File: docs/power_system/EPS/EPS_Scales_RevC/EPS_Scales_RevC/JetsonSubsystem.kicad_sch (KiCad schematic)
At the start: 19 parts, among them U4 INA230

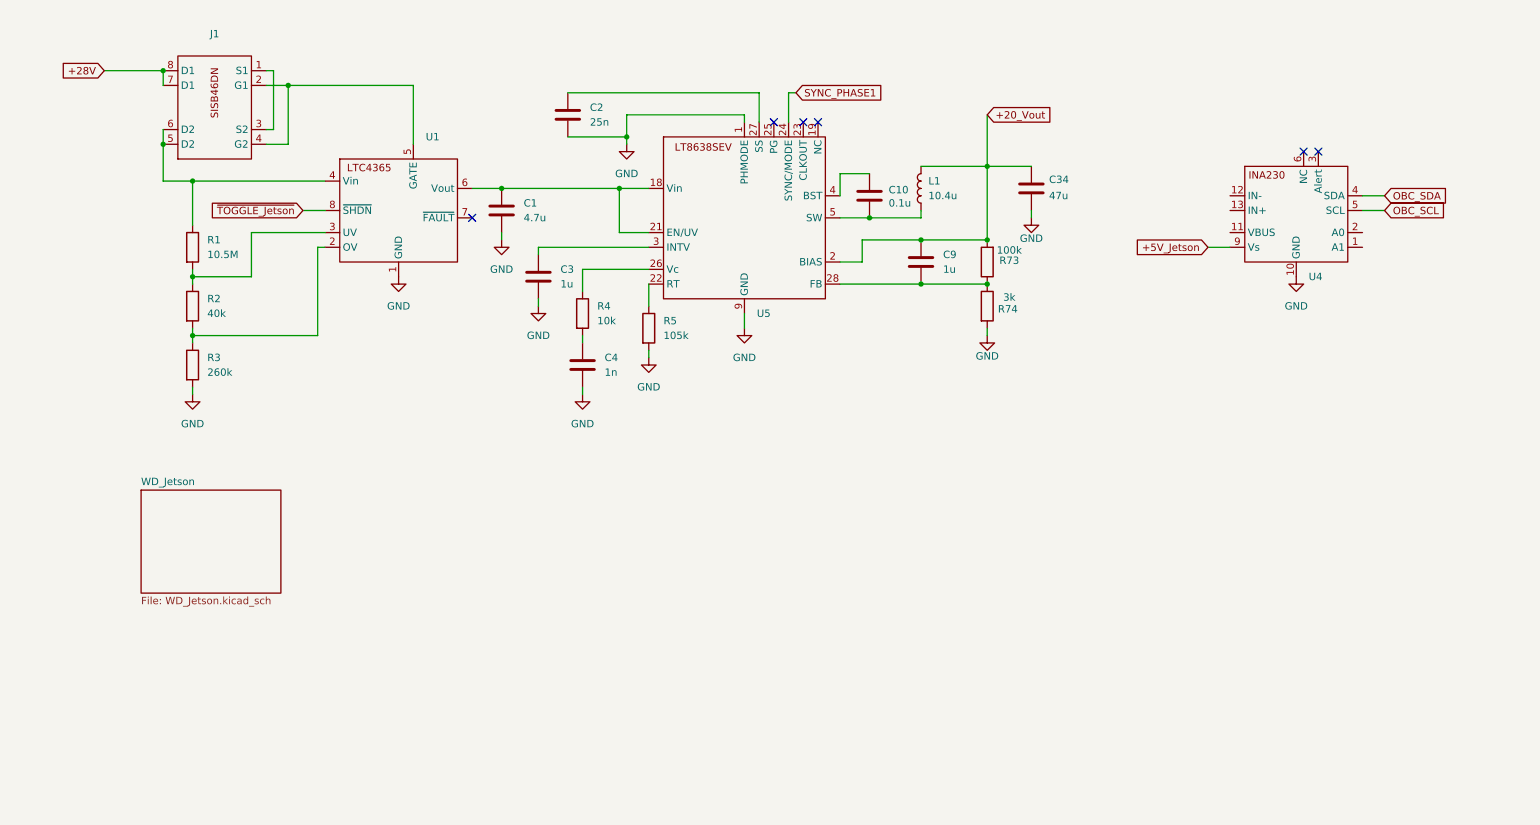
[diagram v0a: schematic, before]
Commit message: Calculations
Lots of behind the scenes stuff going on. Ran through calculations for the Load Switch, Switching Regulator and clock for the jetson using the information from each datasheet. Having to modify these parameters for each subsystem is time consuming as each one requires new calculations. Once this bit is done the schematic will be done, leading to layout. Aiming for thursday Layout.
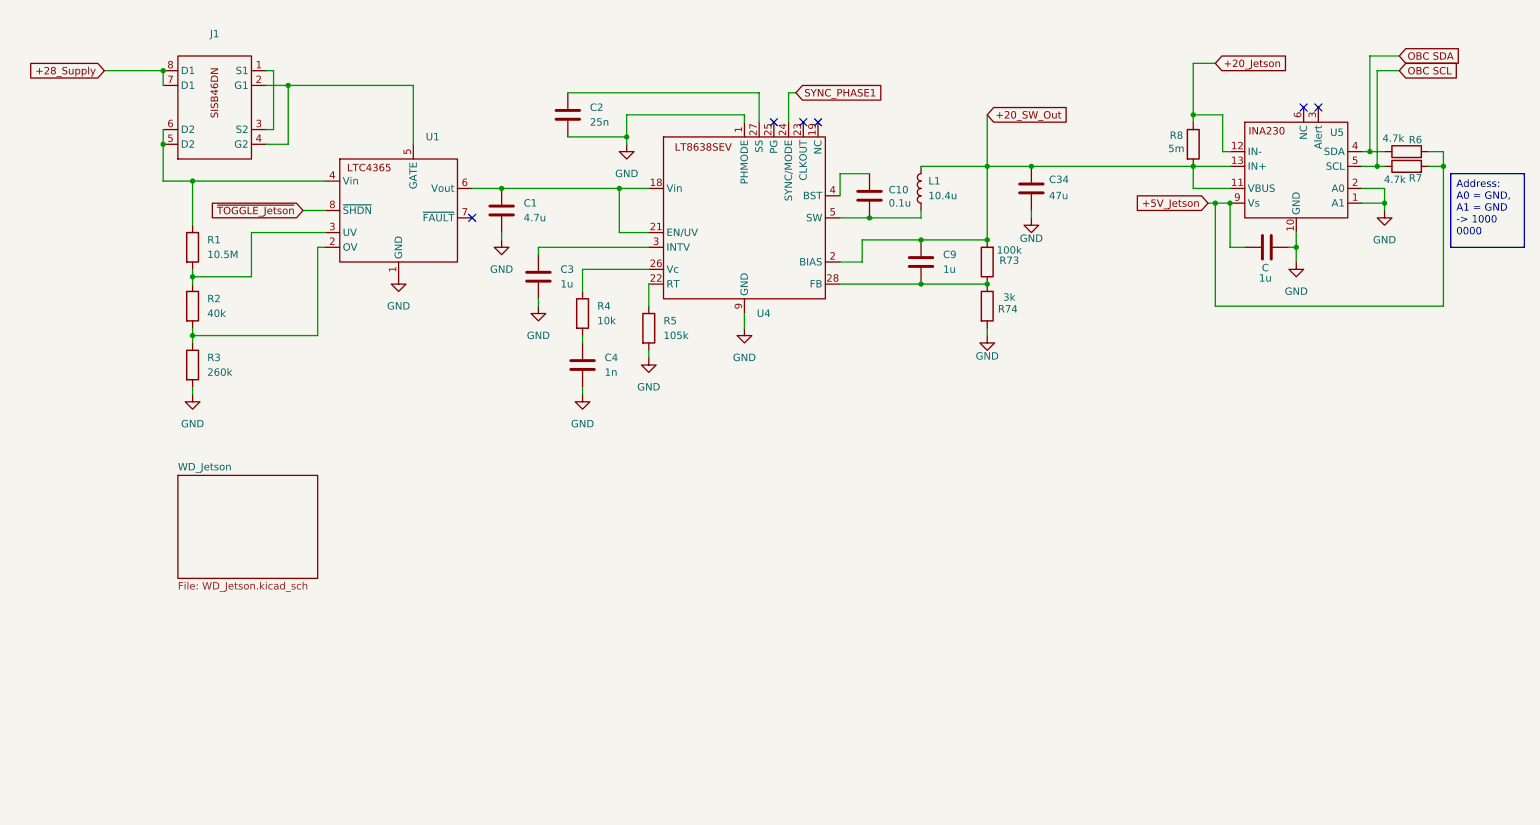
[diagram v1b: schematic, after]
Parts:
- removed U4: INA230, RevC Footprints:INA230AIRGTT, symbol INA230:INA230 [RGT PACKAGE]
- removed U5: ~, RevC Footprints:LT8638SEVPBF, symbol LT8638SEV#PBF:LT863SEV#PBF
- added 1u: C, symbol Device:C
- added R6, R7: 4.7k, symbol Device:R
- added R8: 5m, symbol Device:R
- added U4: ~, RevC Footprints:LT8638SEVPBF, symbol LT8638SEV#PBF:LT863SEV#PBF
- added U5: INA230, RevC Footprints:INA230AIRGTT, symbol INA230:INA230 [RGT PACKAGE]
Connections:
- net +5V_Jetson: now also 1u.2, R6.2, R7.2, U5.9 (Vs)
- net GND: now also 1u.1, U4.1 (PHMODE), U4.9 (GND), U5.1 (A1), U5.10 (GND), U5.2 (A0)
- net SYNC_PHASE1: now also U4.24 (SYNC/MODE)
- net at C1.1, U1.6 (Vout): now also U4.18 (Vin), U4.21 (EN/UV)
- net at C10.1: now also U4.4 (BST)
- net at C10.2, L1.1: now also U4.5 (SW)
- net at R4.1: now also U4.26 (Vc)
- net at C2.1: now also U4.27 (SS)
- net at C3.1: now also U4.3 (INTV)
- net at C9.2, R73.1, R74.1: now also U4.28 (FB)
- net at R5.1: now also U4.22 (RT)
- net +20_Vout renamed +20_SW_Out
- net +20_SW_Out: now also R8.2, U4.2 (BIAS), U5.11 (VBUS), U5.13 (IN+)
- net +28V renamed +28_Supply
- new net +20_Jetson: R8.1, U5.12 (IN-)
- new net OBC SCL: R7.1, U5.5 (SCL)
- new net OBC SDA: R6.1, U5.4 (SDA)

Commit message: Rev C. Schematic 90 % Complete
All EPS components for each subsystem implemented. Only errors and warning are relating to missing peripheral connections and connectors which will be discussed tomorrow when I go to the lab.
Calculations are done as well.
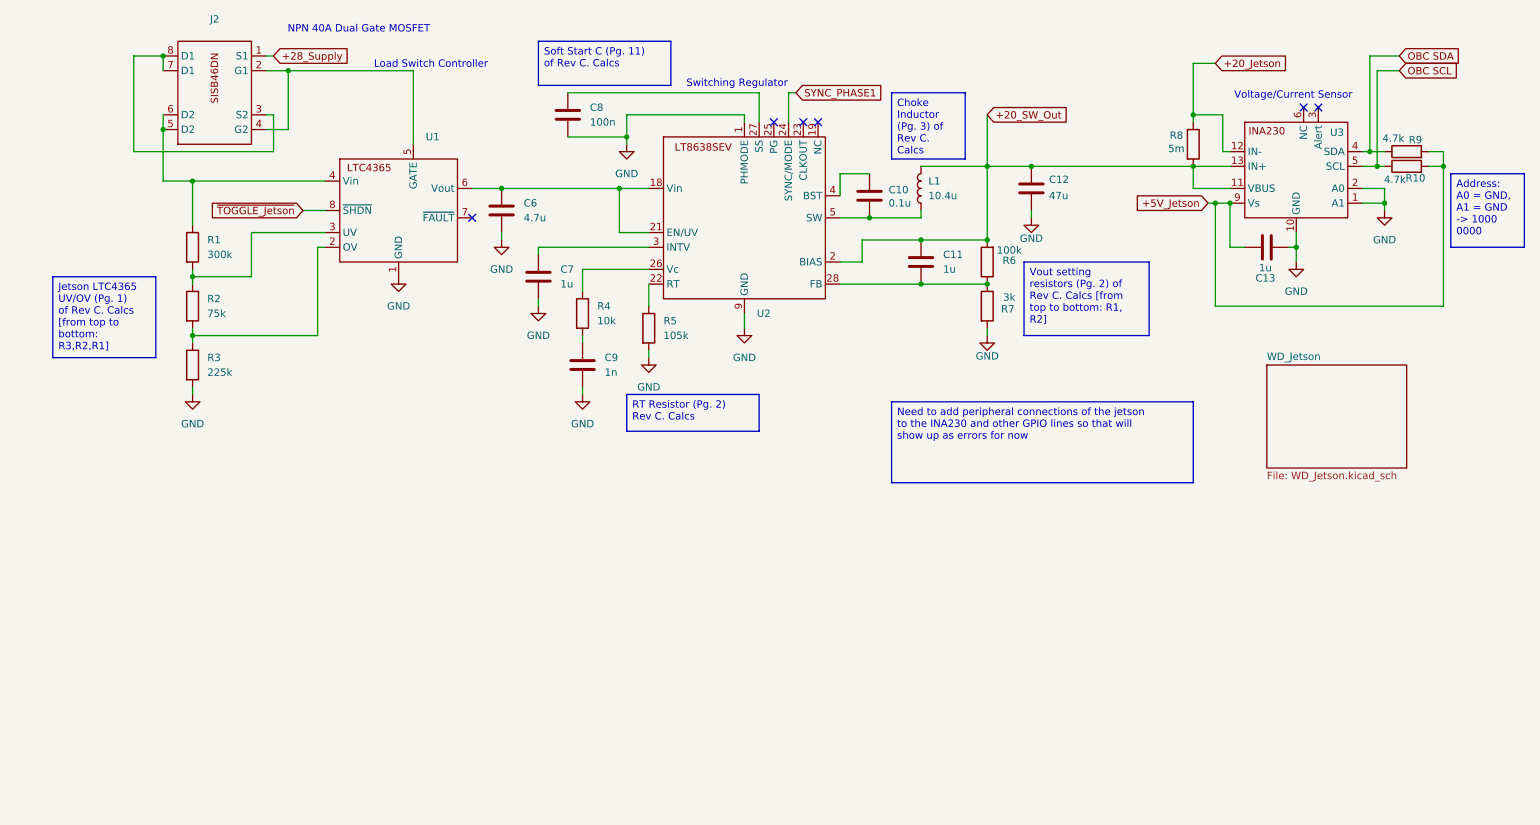
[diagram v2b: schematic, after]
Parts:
- C13: renamed from 1u; value C -> 1u
- C8: renamed from C2; value 25n -> 100n
- R1: value 10.5M -> 300k
- R2: value 40k -> 75k
- R3: value 260k -> 225k
- renumbered C9 to C11, C34 to C12, C1 to C6, C3 to C7, C4 to C9, J1 to J2, R7 to R10, R73 to R6, R74 to R7, R6 to R9, U4 to U2, U5 to U3
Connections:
- net +28_Supply: now also J2.1 (S1); no longer J2.7 (D1), J2.8 (D1)
- net at J2.3 (S2): now also J2.7 (D1), J2.8 (D1); no longer J2.1 (S1)
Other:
- note added: "Load Switch Controller"
- note added: "NPN 40A Dual Gate MOSFET"
- note added: "Switching Regulator"
- note added: "Voltage/Current Sensor"
- moved on the sheet: J2

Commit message: Added Dummy Boards & XNOR functionality
Almost done with Dummy boards, just need to link some gecko footprints to the schematic symbol pins and layout can begin
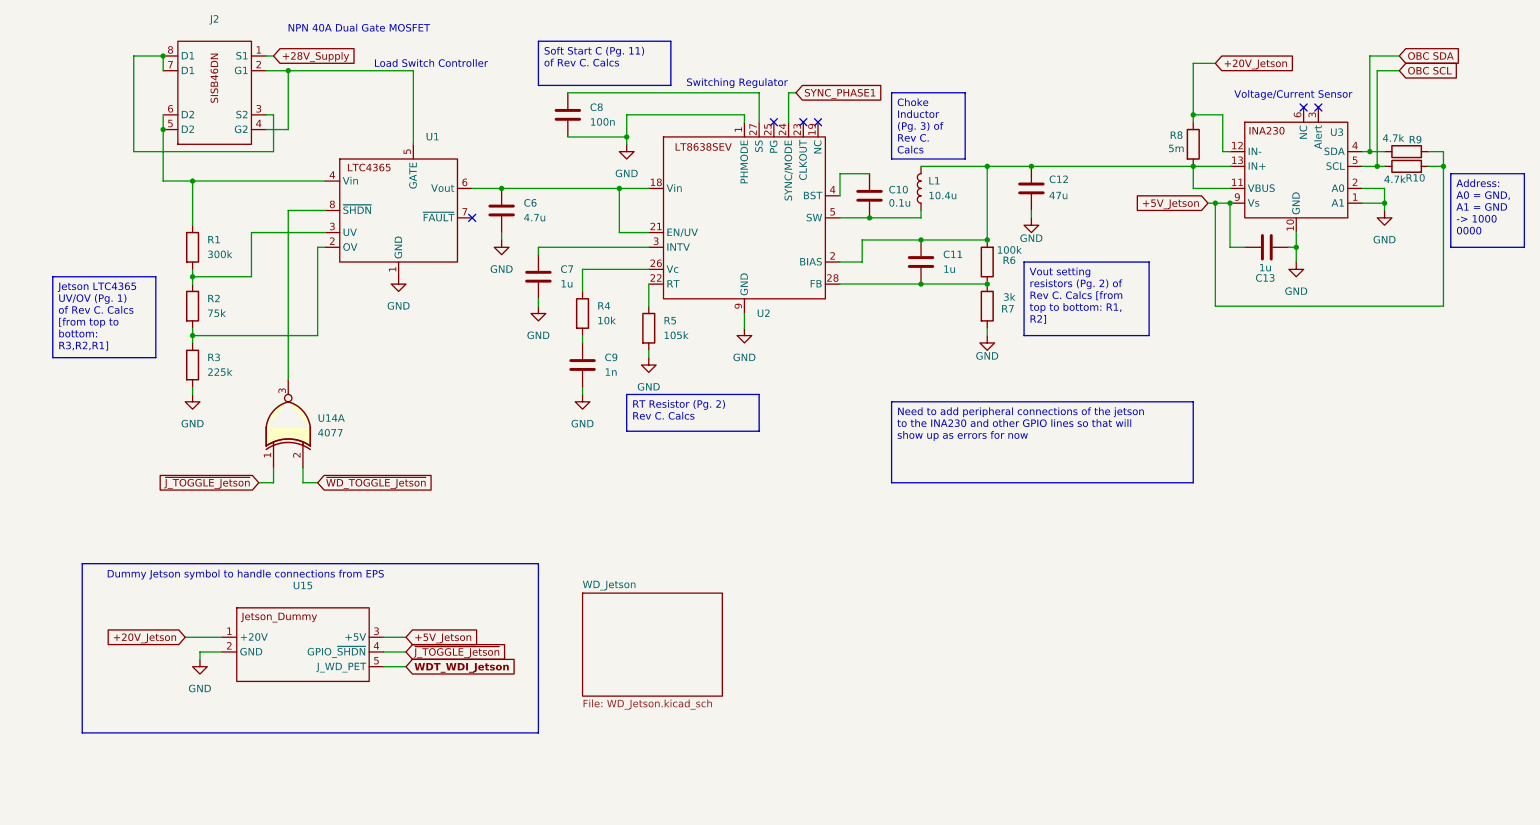
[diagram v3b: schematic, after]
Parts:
- added U14: 4077, symbol 4xxx:4077
- added U15: ~, symbol Jetson_Dummy:Jetson_Dummy
- J2: footprint RevC Footprints:MOSFET_DN-T1-GE3_VIS -> RevC Footprints:SISB46DN-T1-GE3
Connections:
- net +5V_Jetson: now also U15.3 (+5V)
- net GND: now also U15.2 (GND)
- net +20_Jetson renamed +20V_Jetson
- net +20V_Jetson: now also U15.1 (+20V)
- net +20_SW_Out: no longer names the net of C11.1, C12.1, L1.2, R6.2, R8.2, U2.2 (BIAS), U3.11 (VBUS), U3.13 (IN+)
- net +28_Supply renamed +28V_Supply
- net ~{TOGGLE_Jetson}: no longer names the net of U1.8 (~{SHDN})
- net ~{TOGGLE_Jetson}: now also U14.3
- new net WDT_WDI_Jetson: U15.5 (J_WD_PET)
- new net ~{J_TOGGLE_Jetson}: U14.1, U15.4 (GPIO_~{SHDN})
- new net ~{WD_TOGGLE_Jetson}: U14.2
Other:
- note added: "Dummy Jetson symbol to handle connections from EPS"

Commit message: Rev C. Layout Started
Footprints and Symbols properly linked. Started organizing PCB layout
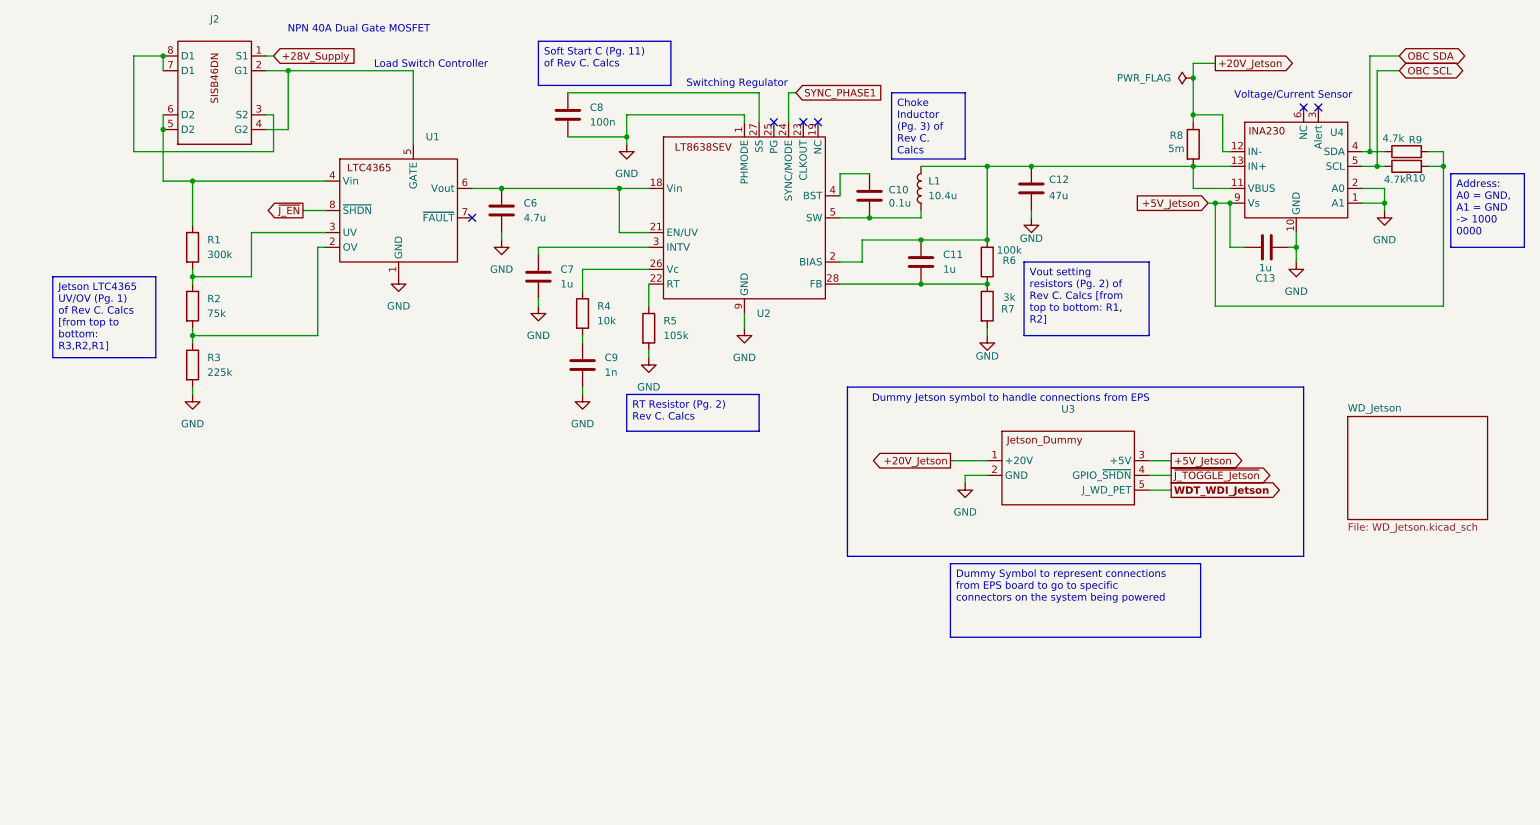
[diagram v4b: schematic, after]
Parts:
- removed U14: 4077, symbol 4xxx:4077
- C10, C11, C12, C13, C6, C7, C8, C9: footprint (none) -> Capacitor_SMD:C_0603_1608Metric
- L1: footprint (none) -> Inductor_SMD:L_0603_1608Metric
- R1, R10, R2, R3, R4, R5, R6, R7, R8, R9: footprint (none) -> Resistor_SMD:R_0603_1608Metric
- U3: renamed from U15; footprint (none) -> Connector_PinSocket_2.54mm:PinSocket_1x05_P2.54mm_Vertical
- renumbered U3 to U4
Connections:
- net ~{J_EN}: now reaches U1.8 (~{SHDN})
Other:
- moved on the sheet: U3

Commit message: Layout Revisions
Organizing components and layering considerations
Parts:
- added J11: G125-MH11605L3P, RevC Footprints:HARWIN_G125-MH11605L3P, symbol 16 Pin Gecko Male Connector:G125-MH11605L3P
- U3: now not fitted; now left out of the parts list
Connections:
- net +20V_Jetson: now also J11.1, J11.2, J11.3, J11.4
- net +5V_Jetson: now also J11.10, J11.9
- net GND: now also J11.17 (SH1), J11.18 (SH2), J11.5, J11.6, J11.7, J11.8
- net WDT_WDI_Jetson: now also J11.15, J11.16
- net ~{J_TOGGLE_Jetson}: now also J11.13, J11.14
- no-connect marks 6 -> 8
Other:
- note added: "Gecko 16 pin Male connector"
- note added: "Gecko Connector to interface with Jetson to EPS"
- note removed: "Dummy Jetson symbol to handle connections from EPS"
